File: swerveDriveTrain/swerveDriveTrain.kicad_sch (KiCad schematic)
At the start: 41 parts, among them IC1 TCAN3414DR, J1 RJ45, J2 Screw_Terminal_01x02, J3 Conn_01x06_Pin, J4 S6B-PH-K-S_LF__SN_, P1 USB_C_Plug_USB2.0, U2 Teensy4.0

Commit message: first layout pass
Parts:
- TP1, TP10, TP11, TP12, TP13, TP14, TP15, TP16, TP17, TP2, TP3, TP4, TP5, TP6, TP7, TP8, TP9: footprint TestPoint:TestPoint_Pad_D4.0mm -> TestPoint:TestPoint_Pad_D1.5mm
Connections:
- net CANH renamed CANP
- net CANL renamed CANN
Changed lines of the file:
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@@
 		)
 	)
-	(global_label "CANL"
+	(global_label "CANN"
 		(shape input)
 		(at 262.89 33.02 180)
@@
 		)
 		(property "Intersheetrefs" "${INTERSHEET_REFS}"
-			(at 255.1876 33.02 0)
+			(at 255.5394 33.02 0)
 			(effects
 				(font
@@
 		)
 	)
-	(global_label "CANH"
+	(global_label "CANP"
 		(shape input)
 		(at 262.89 27.94 180)
@@
 		)
 		(property "Intersheetrefs" "${INTERSHEET_REFS}"
-			(at 254.8852 27.94 0)
+			(at 255.5999 27.94 0)
 			(effects
 				(font
@@
 		)
 	)
-	(global_label "CANL"
+	(global_label "CANN"
 		(shape input)
 		(at 33.02 29.21 0)
@@
 		)
 		(property "Intersheetrefs" "${INTERSHEET_REFS}"
-			(at 40.7224 29.21 0)
+			(at 40.3706 29.21 0)
 			(effects
 				(font
@@
 		)
 	)
-	(global_label "CANH"
+	(global_label "CANP"
 		(shape input)
 		(at 148.59 177.8 0)
@@
 		)
 		(property "Intersheetrefs" "${INTERSHEET_REFS}"
-			(at 156.5948 177.8 0)
+			(at 155.8801 177.8 0)
 			(effects
 				(font
@@
 		)
 	)
-	(global_label "CANH"
+	(global_label "CANP"
 		(shape input)
 		(at 33.02 31.75 0)
@@
 		)
 		(property "Intersheetrefs" "${INTERSHEET_REFS}"
-			(at 41.0248 31.75 0)
+			(at 40.3101 31.75 0)
 			(effects
 				(font
@@
 		)
 	)
-	(global_label "CANL"
+	(global_label "CANN"
 		(shape input)
 		(at 148.59 180.34 0)
@@
 		)
 		(property "Intersheetrefs" "${INTERSHEET_REFS}"
-			(at 156.2924 180.34 0)
+			(at 155.9406 180.34 0)
 			(effects
 				(font
@@
 			)
 		)
-		(property "Footprint" "TestPoint:TestPoint_Pad_D4.0mm"
+		(property "Footprint" "TestPoint:TestPoint_Pad_D1.5mm"
 			(at 267.97 17.78 0)
 			(effects
@@
 			)
 		)
-		(property "Footprint" "TestPoint:TestPoint_Pad_D4.0mm"
+		(property "Footprint" "TestPoint:TestPoint_Pad_D1.5mm"
 			(at 267.97 78.74 0)
 			(effects
@@
 			)
 		)
-		(property "Footprint" "TestPoint:TestPoint_Pad_D4.0mm"
+		(property "Footprint" "TestPoint:TestPoint_Pad_D1.5mm"
 			(at 267.97 83.82 0)
 			(effects
@@
 			)
 		)
-		(property "Footprint" "TestPoint:TestPoint_Pad_D4.0mm"
+		(property "Footprint" "TestPoint:TestPoint_Pad_D1.5mm"
 			(at 267.97 63.5 0)
 			(effects
@@
 			)
 		)
-		(property "Footprint" "TestPoint:TestPoint_Pad_D4.0mm"
+		(property "Footprint" "TestPoint:TestPoint_Pad_D1.5mm"
 			(at 267.97 100.33 0)
 			(effects
@@
 			)
 		)
-		(property "Footprint" "TestPoint:TestPoint_Pad_D4.0mm"
+		(property "Footprint" "TestPoint:TestPoint_Pad_D1.5mm"
 			(at 267.97 48.26 0)
 			(effects
@@
 			)
 		)
-		(property "Footprint" "TestPoint:TestPoint_Pad_D4.0mm"
+		(property "Footprint" "TestPoint:TestPoint_Pad_D1.5mm"
 			(at 267.97 68.58 0)
 			(effects
@@
 			)
 		)
-		(property "Footprint" "TestPoint:TestPoint_Pad_D4.0mm"
+		(property "Footprint" "TestPoint:TestPoint_Pad_D1.5mm"
 			(at 267.97 38.1 0)
 			(effects
@@
 			)
 		)
-		(property "Footprint" "TestPoint:TestPoint_Pad_D4.0mm"
+		(property "Footprint" "TestPoint:TestPoint_Pad_D1.5mm"
 			(at 267.97 27.94 0)
 			(effects
@@
 			)
 		)
-		(property "Footprint" "TestPoint:TestPoint_Pad_D4.0mm"
+		(property "Footprint" "TestPoint:TestPoint_Pad_D1.5mm"
 			(at 267.97 93.98 0)
 			(effects
@@
 			)
 		)
-		(property "Footprint" "TestPoint:TestPoint_Pad_D4.0mm"
+		(property "Footprint" "TestPoint:TestPoint_Pad_D1.5mm"
 			(at 267.97 73.66 0)
 			(effects
@@
 			)
 		)
-		(property "Footprint" "TestPoint:TestPoint_Pad_D4.0mm"
+		(property "Footprint" "TestPoint:TestPoint_Pad_D1.5mm"
 			(at 267.97 53.34 0)
 			(effects
@@
 			)
 		)
-		(property "Footprint" "TestPoint:TestPoint_Pad_D4.0mm"
+		(property "Footprint" "TestPoint:TestPoint_Pad_D1.5mm"
 			(at 267.97 43.18 0)
 			(effects
@@
 			)
 		)
-		(property "Footprint" "TestPoint:TestPoint_Pad_D4.0mm"
+		(property "Footprint" "TestPoint:TestPoint_Pad_D1.5mm"
 			(at 267.97 88.9 0)
 			(effects
@@
 			)
 		)
-		(property "Footprint" "TestPoint:TestPoint_Pad_D4.0mm"
+		(property "Footprint" "TestPoint:TestPoint_Pad_D1.5mm"
 			(at 267.97 33.02 0)
 			(effects
@@
 			)
 		)
-		(property "Footprint" "TestPoint:TestPoint_Pad_D4.0mm"
+		(property "Footprint" "TestPoint:TestPoint_Pad_D1.5mm"
 			(at 267.97 22.86 0)
 			(effects
@@
 			)
 		)
-		(property "Footprint" "TestPoint:TestPoint_Pad_D4.0mm"
+		(property "Footprint" "TestPoint:TestPoint_Pad_D1.5mm"
 			(at 267.97 58.42 0)
 			(effects

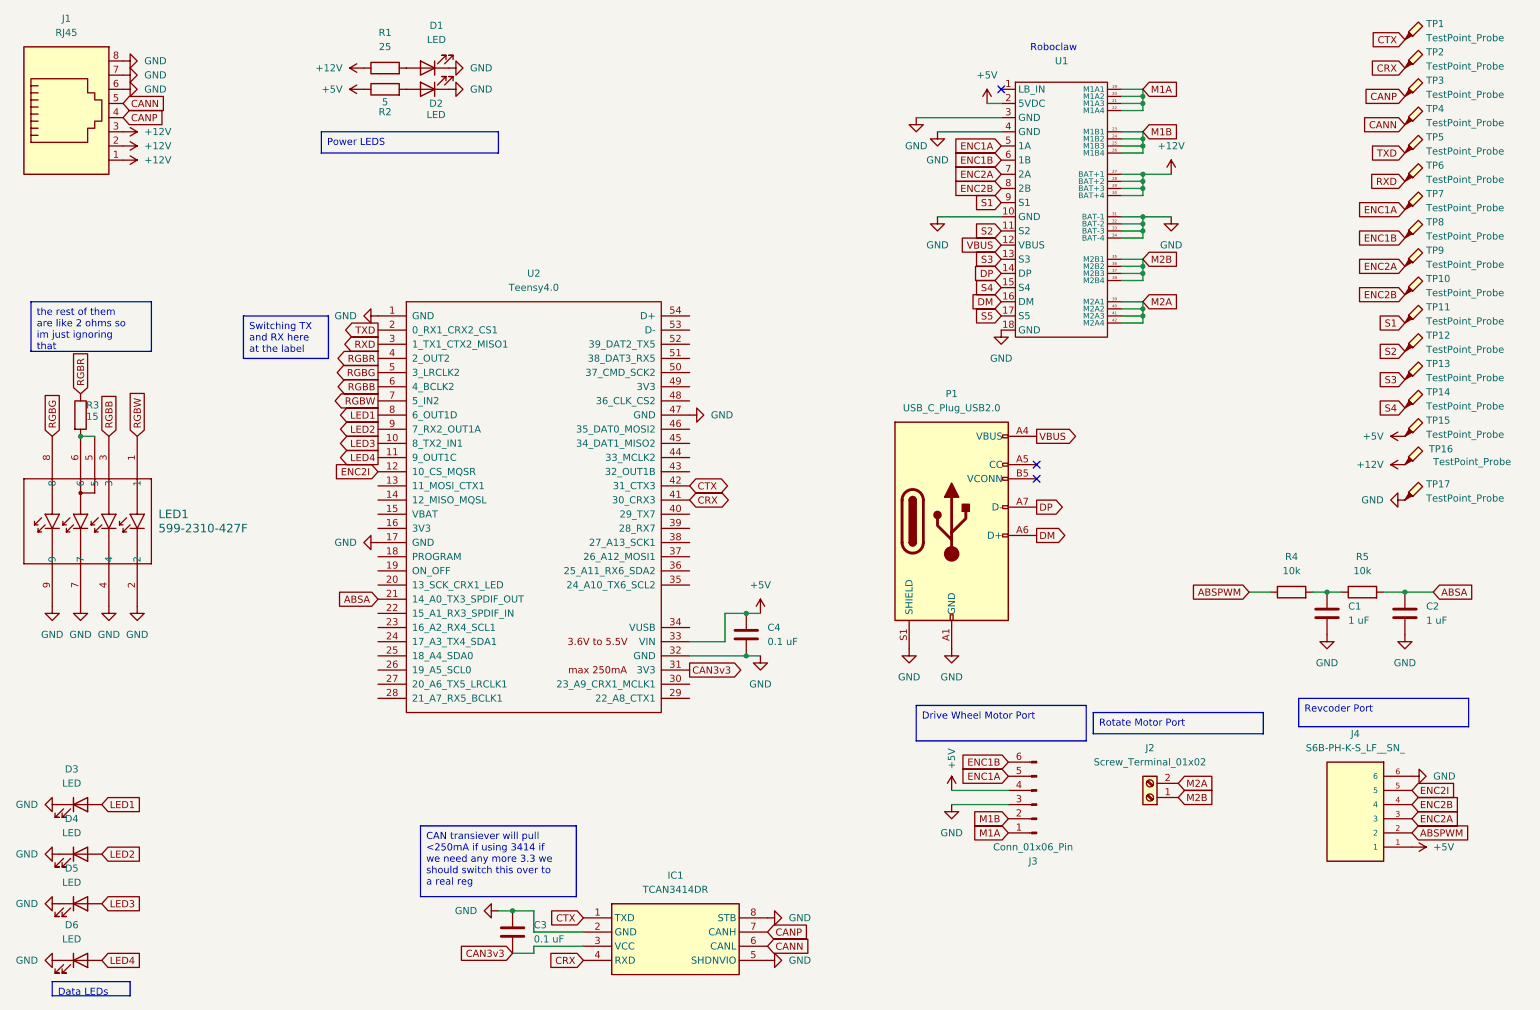
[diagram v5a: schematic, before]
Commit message: layout and routing for swerve
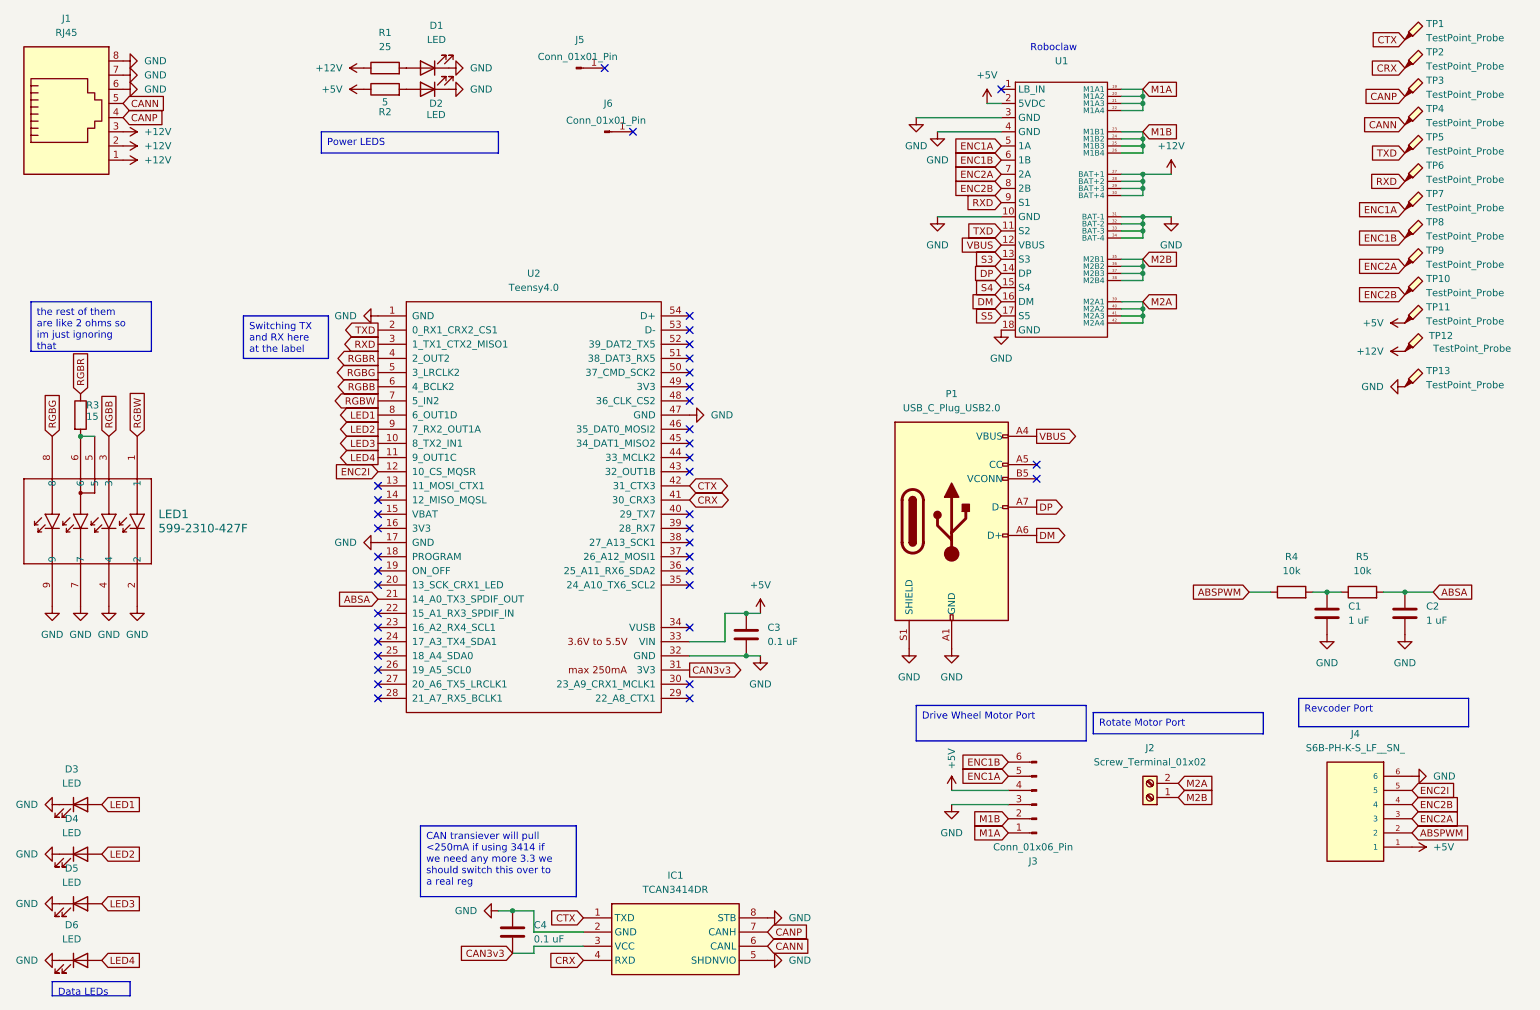
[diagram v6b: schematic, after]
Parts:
- removed TP11, TP12, TP13, TP14: TestPoint_Probe, TestPoint:TestPoint_Pad_D1.5mm, symbol Connector:TestPoint_Probe
- added J5: Conn_01x01_Pin, footprints:Logo_Small, symbol Connector:Conn_01x01_Pin
- added J6: Conn_01x01_Pin, footprints:bird, symbol Connector:Conn_01x01_Pin
- renumbered C4 to C3, C3 to C4, TP15 to TP11, TP16 to TP12, TP17 to TP13
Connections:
- net S1 is gone; now on net RXD: U1.9 (S1)
- net S2 is gone; now on net TXD: U1.11 (S2)
- no-connect marks 3 -> 39
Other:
- moved on the sheet: TP11, TP12, TP13

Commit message: update schematic and make a blank pcb layout for testing
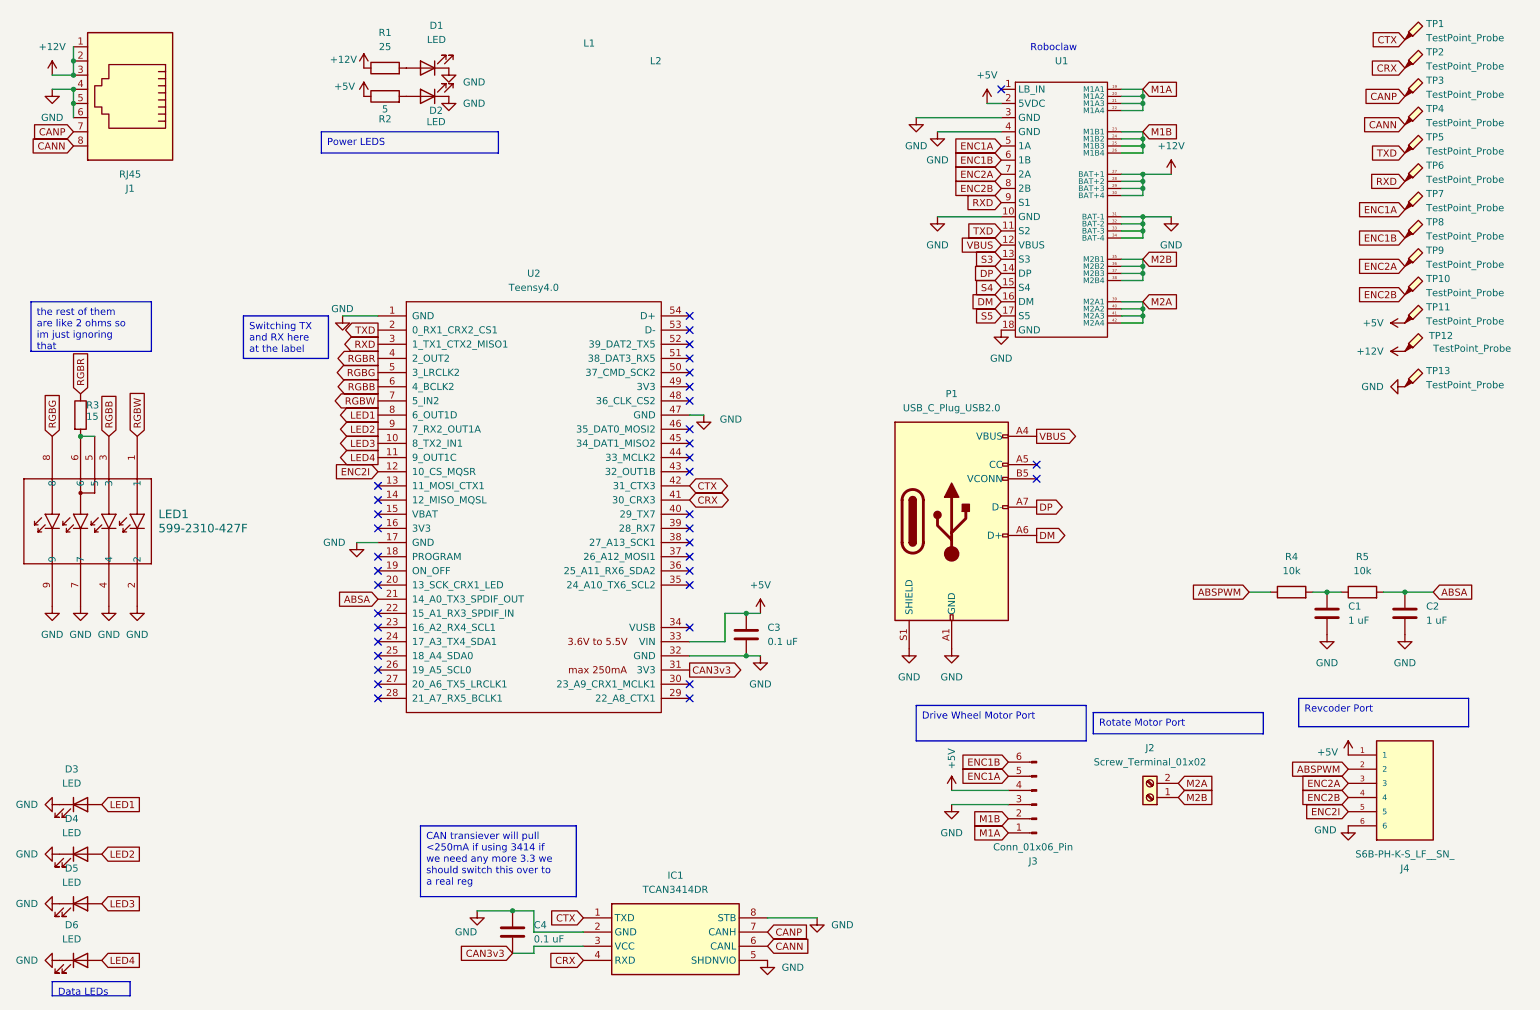
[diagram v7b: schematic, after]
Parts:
- removed J5: Conn_01x01_Pin, footprints:Logo_Small, symbol Connector:Conn_01x01_Pin
- removed J6: Conn_01x01_Pin, footprints:bird, symbol Connector:Conn_01x01_Pin
- added L1: ~, footprints:Logo_Small, symbol custom:Logo
- added L2: ~, footprints:bird, symbol custom:Logo
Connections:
- net CANN: now also J1.8; no longer J1.5
- net CANP: now also J1.7; no longer J1.4
- net GND: now also J1.4, J1.5; no longer J1.7, J1.8
- no-connect marks 39 -> 37
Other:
- moved on the sheet: D2, J1, J4, R2

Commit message: switched motor drivers out schematic and footprint
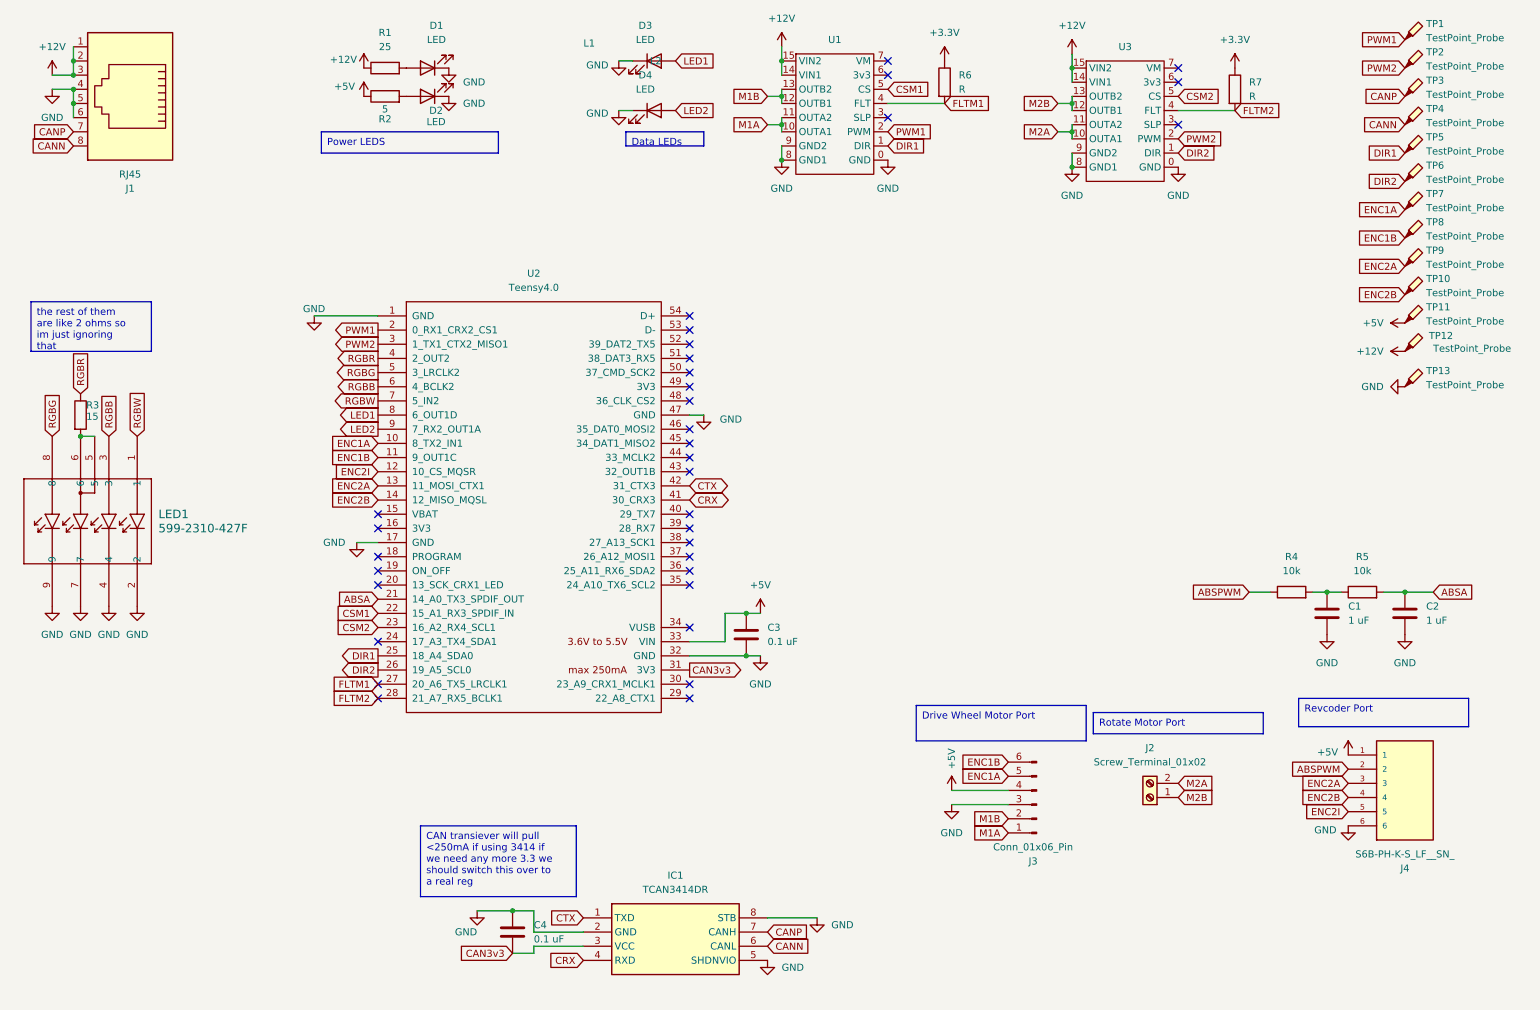
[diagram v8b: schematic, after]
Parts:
- removed D5, D6: LED, GreenLED:LED_CREE_MLXXXX, symbol Device:LED
- removed P1: USB_C_Plug_USB2.0, Connector_USB:USB_C_Receptacle_GCT_USB4085, symbol Connector:USB_C_Plug_USB2.0
- removed U1: ~, Custom:roboclaw, symbol roboclaw:Roboclaw
- added R6, R7: R, Resistor_SMD:R_0805_2012Metric_Pad1.20x1.40mm_HandSolder, symbol Device:R
- added U1, U3: ~, footprints:G218v17, symbol custom:G218v17
- J1: footprint Connector_RJ:RJ45_Amphenol_54602-x08_Horizontal -> Connector_RJ:RJ45_OST_PJ012-8P8CX_Vertical
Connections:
- net LED3 is gone; now on net ENC1A: U2.10 (8_TX2_IN1)
- net LED4 is gone; now on net ENC1B: U2.11 (9_OUT1C)
- net +12V: now also U1.14 (VIN1), U1.15 (VIN2), U3.14 (VIN1), U3.15 (VIN2)
- net CRX: no longer TP2.1
- net CTX: no longer TP1.1
- net ENC2A: now also U2.13 (11_MOSI_CTX1)
- net ENC2B: now also U2.14 (12_MISO_MQSL)
- net GND: now also U1.0 (GND), U1.8 (GND1), U1.9 (GND2), U3.0 (GND), U3.8 (GND1), U3.9 (GND2)
- net M1A: now also U1.10 (OUTA1), U1.11 (OUTA2)
- net M1B: now also U1.12 (OUTB1), U1.13 (OUTB2)
- net M2A: now also U3.10 (OUTA1), U3.11 (OUTA2)
- net M2B: now also U3.12 (OUTB1), U3.13 (OUTB2)
- net CSM1: now reaches U2.22 (15_A1_RX3_SPDIF_IN)
- net CSM1: now also U1.5 (CS)
- net CSM2: now reaches U2.23 (16_A2_RX4_SCL1)
- net CSM2: now also U3.5 (CS)
- net DIR1: now reaches U2.25 (18_A4_SDA0)
- net DIR1: now also TP5.1, U1.1 (DIR)
- net DIR2: now reaches U2.26 (19_A5_SCL0)
- net DIR2: now also TP6.1, U3.1 (DIR)
- net FLTM1: now reaches U2.27 (20_A6_TX5_LRCLK1)
- net FLTM1: now also R6.2, U1.4 (FLT)
- net FLTM2: now reaches U2.28 (21_A7_RX5_BCLK1)
- net FLTM2: now also R7.2, U3.4 (FLT)
- net RXD renamed PWM2
- net PWM2: now also TP2.1, U3.2 (PWM); no longer TP6.1
- net TXD renamed PWM1
- net PWM1: now also TP1.1, U1.2 (PWM); no longer TP5.1
- new net +3.3V: R6.1, R7.1
- no-connect marks 37 -> 34
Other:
- note removed: "Roboclaw"
- moved on the sheet: D3, D4
